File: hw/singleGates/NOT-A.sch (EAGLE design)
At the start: 3 parts, among them Q1 BC817

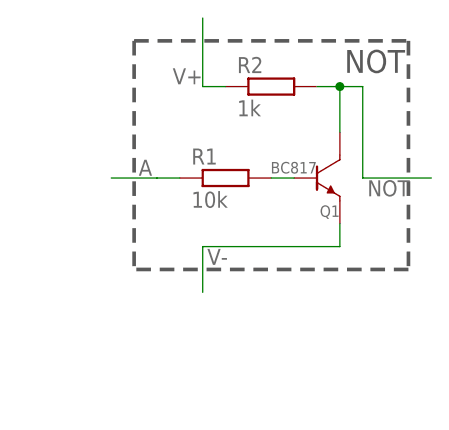
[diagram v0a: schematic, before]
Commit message: Updated gates to be centered
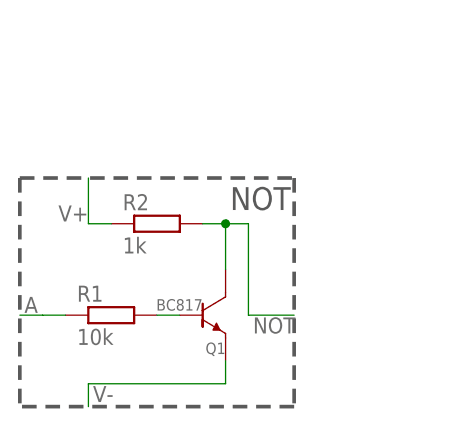
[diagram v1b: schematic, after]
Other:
- moved on the sheet: Q1, R1, R2
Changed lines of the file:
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@@
 <sheet>
 <plain>
-<wire x1="33.02" y1="2.54" x2="2.54" y2="2.54" width="0.4064" layer="97" style="longdash"/>
-<wire x1="2.54" y1="27.94" x2="2.54" y2="2.54" width="0.4064" layer="97" style="longdash"/>
-<wire x1="33.02" y1="27.94" x2="33.02" y2="2.54" width="0.4064" layer="97" style="longdash"/>
-<wire x1="2.54" y1="27.94" x2="33.02" y2="27.94" width="0.4064" layer="97" style="longdash"/>
-<text x="25.908" y="24.384" size="2.54" layer="97" ratio="12">NOT</text>
+<wire x1="20.32" y1="-12.7" x2="-10.16" y2="-12.7" width="0.4064" layer="97" style="longdash"/>
+<wire x1="-10.16" y1="12.7" x2="-10.16" y2="-12.7" width="0.4064" layer="97" style="longdash"/>
+<wire x1="20.32" y1="12.7" x2="20.32" y2="-12.7" width="0.4064" layer="97" style="longdash"/>
+<wire x1="-10.16" y1="12.7" x2="20.32" y2="12.7" width="0.4064" layer="97" style="longdash"/>
+<text x="13.208" y="9.144" size="2.54" layer="97" ratio="12">NOT</text>
 </plain>
 <instances>
-<instance part="R1" gate="G$1" x="12.7" y="12.7"/>
-<instance part="R2" gate="G$1" x="17.78" y="22.86"/>
-<instance part="Q1" gate="G$1" x="25.4" y="12.7" smashed="yes">
-<attribute name="NAME" x="25.4" y="8.382" size="1.27" layer="95" ratio="12" rot="R180" align="top-left"/>
-<attribute name="VALUE" x="22.86" y="14.478" size="1.27" layer="96" ratio="12" rot="R180"/>
+<instance part="R1" gate="G$1" x="0" y="-2.54"/>
+<instance part="R2" gate="G$1" x="5.08" y="7.62"/>
+<instance part="Q1" gate="G$1" x="12.7" y="-2.54" smashed="yes">
+<attribute name="NAME" x="12.7" y="-6.858" size="1.27" layer="95" ratio="12" rot="R180" align="top-left"/>
+<attribute name="VALUE" x="10.16" y="-0.762" size="1.27" layer="96" ratio="12" rot="R180"/>
 </instance>
 </instances>
@@
 <net name="V-" class="0">
 <segment>
-<wire x1="10.16" y1="5.08" x2="25.4" y2="5.08" width="0.1524" layer="91"/>
-<wire x1="25.4" y1="5.08" x2="25.4" y2="7.62" width="0.1524" layer="91"/>
-<label x="10.668" y="3.048" size="1.778" layer="95"/>
-<wire x1="10.16" y1="5.08" x2="10.16" y2="0" width="0.1524" layer="91"/>
+<wire x1="-2.54" y1="-10.16" x2="12.7" y2="-10.16" width="0.1524" layer="91"/>
+<wire x1="12.7" y1="-10.16" x2="12.7" y2="-7.62" width="0.1524" layer="91"/>
+<label x="-2.032" y="-12.192" size="1.778" layer="95"/>
+<wire x1="-2.54" y1="-10.16" x2="-2.54" y2="-12.7" width="0.1524" layer="91"/>
 <pinref part="Q1" gate="G$1" pin="EMITTER"/>
 </segment>
@@
 <segment>
 <pinref part="R1" gate="G$1" pin="2"/>
-<wire x1="17.78" y1="12.7" x2="20.32" y2="12.7" width="0.1524" layer="91"/>
+<wire x1="5.08" y1="-2.54" x2="7.62" y2="-2.54" width="0.1524" layer="91"/>
 <pinref part="Q1" gate="G$1" pin="BASE"/>
 </segment>
@@
 <net name="NOT" class="0">
 <segment>
-<wire x1="25.4" y1="17.78" x2="25.4" y2="22.86" width="0.1524" layer="91"/>
-<wire x1="25.4" y1="22.86" x2="27.94" y2="22.86" width="0.1524" layer="91"/>
-<wire x1="27.94" y1="22.86" x2="27.94" y2="12.7" width="0.1524" layer="91"/>
-<wire x1="27.94" y1="12.7" x2="35.56" y2="12.7" width="0.1524" layer="91"/>
-<label x="28.448" y="10.668" size="1.778" layer="95"/>
+<wire x1="12.7" y1="2.54" x2="12.7" y2="7.62" width="0.1524" layer="91"/>
+<wire x1="12.7" y1="7.62" x2="15.24" y2="7.62" width="0.1524" layer="91"/>
+<wire x1="15.24" y1="7.62" x2="15.24" y2="-2.54" width="0.1524" layer="91"/>
+<wire x1="15.24" y1="-2.54" x2="20.32" y2="-2.54" width="0.1524" layer="91"/>
+<label x="15.748" y="-4.572" size="1.778" layer="95"/>
 <pinref part="R2" gate="G$1" pin="2"/>
-<wire x1="25.4" y1="22.86" x2="22.86" y2="22.86" width="0.1524" layer="91"/>
-<junction x="25.4" y="22.86"/>
+<wire x1="12.7" y1="7.62" x2="10.16" y2="7.62" width="0.1524" layer="91"/>
+<junction x="12.7" y="7.62"/>
 <pinref part="Q1" gate="G$1" pin="COLLECTOR"/>
 </segment>
@@
 <segment>
 <pinref part="R1" gate="G$1" pin="1"/>
-<wire x1="7.62" y1="12.7" x2="5.08" y2="12.7" width="0.1524" layer="91"/>
-<wire x1="5.08" y1="12.7" x2="0" y2="12.7" width="0.1524" layer="91"/>
-<label x="3.048" y="12.954" size="1.778" layer="95"/>
+<wire x1="-5.08" y1="-2.54" x2="-7.62" y2="-2.54" width="0.1524" layer="91"/>
+<wire x1="-7.62" y1="-2.54" x2="-10.16" y2="-2.54" width="0.1524" layer="91"/>
+<label x="-9.652" y="-2.286" size="1.778" layer="95"/>
 </segment>
 </net>
@@
 <segment>
 <pinref part="R2" gate="G$1" pin="1"/>
-<wire x1="12.7" y1="22.86" x2="10.16" y2="22.86" width="0.1524" layer="91"/>
-<wire x1="10.16" y1="22.86" x2="10.16" y2="30.48" width="0.1524" layer="91"/>
-<label x="10.16" y="24.892" size="1.778" layer="95" rot="R180"/>
+<wire x1="0" y1="7.62" x2="-2.54" y2="7.62" width="0.1524" layer="91"/>
+<wire x1="-2.54" y1="7.62" x2="-2.54" y2="12.7" width="0.1524" layer="91"/>
+<label x="-2.54" y="9.652" size="1.778" layer="95" rot="R180"/>
 </segment>
 </net>

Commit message: Updated supply line names to be more spice compatible
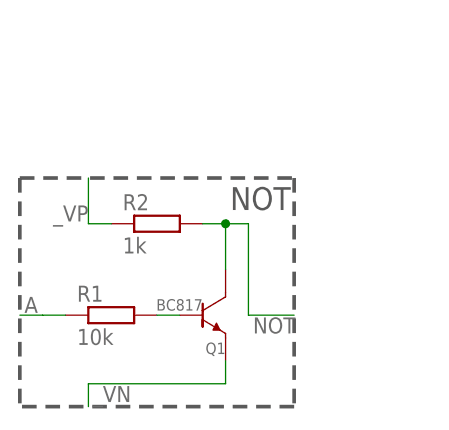
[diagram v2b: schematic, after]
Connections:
- net V+ renamed _VP
- net V- renamed _VN
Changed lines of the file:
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@@
 <?xml version="1.0" encoding="utf-8"?>
 <!DOCTYPE eagle SYSTEM "eagle.dtd">
-<eagle version="7.4.0">
+<eagle version="7.3.0">
 <drawing>
 <settings>
@@
 </busses>
 <nets>
-<net name="V-" class="0">
+<net name="_VN" class="0">
 <segment>
 <wire x1="-2.54" y1="-10.16" x2="12.7" y2="-10.16" width="0.1524" layer="91"/>
@@
 </segment>
 </net>
-<net name="V+" class="0">
+<net name="_VP" class="0">
 <segment>
 <pinref part="R2" gate="G$1" pin="1"/>
